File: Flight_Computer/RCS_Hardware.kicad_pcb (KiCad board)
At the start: 2 copper layers, 60 x 53.1 mm, 55 parts, among them J1 SWD, J2 TYPE-C-31-M-12, J4 5V, J5 GND, J8 Conn_01x05_Male, U1 STM32F401CCU6, U2 AMS1117-3.3, U4 BNO055, U5 W25Q32JVSS, U6 MPU-6050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

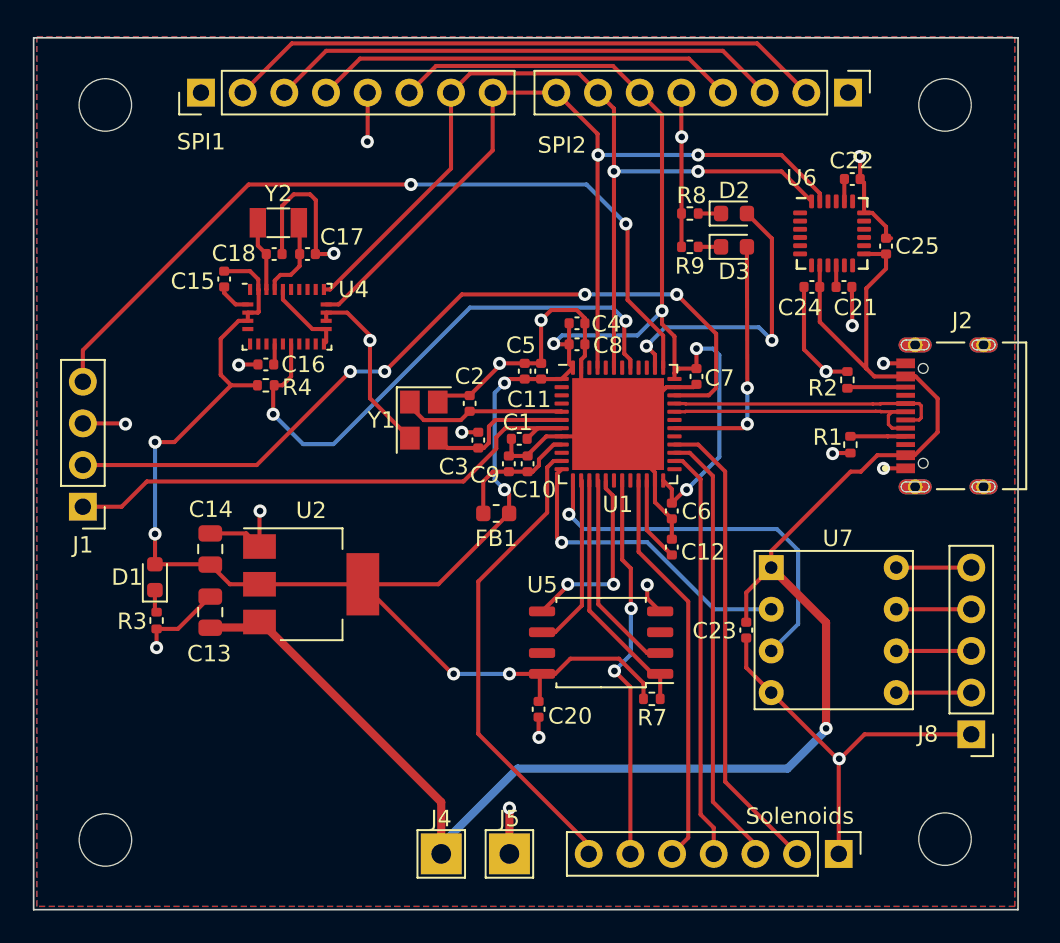
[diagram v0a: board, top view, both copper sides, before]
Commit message: moved some stuff around to aesthetics
moved linear reg down, bottom edge cut & holes up.
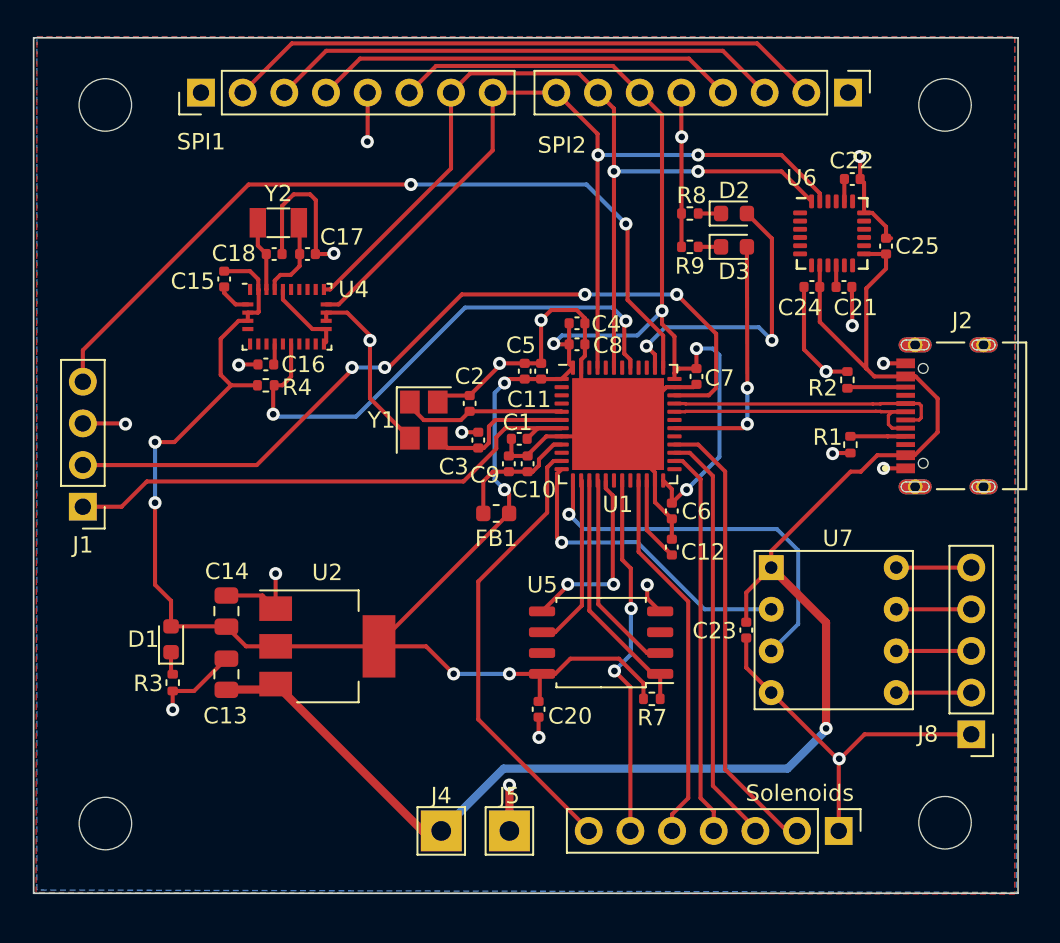
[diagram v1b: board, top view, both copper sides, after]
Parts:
- moved C13 3.91 mm to (113.3, 114.5)
- moved D1 3.91 mm to (110.0, 112.3)
- moved R3 3.91 mm to (110.1, 115.0)
- moved U2 3.91 mm to (119.5, 112.8)
- moved C14 3.91 mm to (113.3, 110.6)
- moved J4 1.40 mm to (126.4, 124.0)
- moved J5 1.40 mm to (130.6, 124.0)
- moved Solenoids 1.40 mm to (150.7, 124.0)
- moved H3 1.00 mm to (106.0, 123.5)
- moved H4 1.00 mm to (157.2, 123.5)
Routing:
- net VBUS: track 102.9 -> 96.4 mm
- net +3.3V: track 146.8 -> 149.2 mm
- net /S6: track 29.4 -> 27.9 mm
- net GND: track 145.5 -> 144.1 mm
- net /S5: track 27.0 -> 25.6 mm
- net /S4: track 25.2 -> 23.8 mm
- net /S3: track 24.4 -> 23.0 mm
- net /BNO_NRST: track 34.1 -> 32.7 mm
- net /S1: track 28.5 -> 27.7 mm
- net /S2: track 23.2 -> 22.4 mm
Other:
- board size 60 x 53.1 mm -> 60 x 52.1 mm

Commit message: uploaded 3d model for components
UCB-C, LTC and Flash Storage
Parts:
- renumbered U7 to LTC
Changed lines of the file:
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@@
     (property "Sheetname" "")
     (attr through_hole)
-    (fp_text reference "U7" (at 4.064 -1.778 unlocked) (layer "F.SilkS")
+    (fp_text reference "LTC" (at 4.064 -1.778 unlocked) (layer "F.SilkS")
         (effects (font (size 1 1) (thickness 0.15)))
     )
@@
     (pad "8" thru_hole circle (at 7.62 0) (size 1.524 1.524) (drill 0.762) (layers "*.Cu" "*.Mask")
       (net 48 "Net-(J8-Pin_5)") (pinfunction "A") (pintype "input"))
+    (model "${KIPRJMOD}/Components/LT1690/LTC1690IN8#PBF.STEP"
+      (offset (xyz 7.6 -7.6 0))
+      (scale (xyz 1 1 1))
+      (rotate (xyz -90 0 0))
+    )
   )
   (footprint "TestPoint:TestPoint_THTPad_2.5x2.5mm_Drill1.2mm" (layer "F.Cu")
@@
     )
     (fp_text user "PCB EDGE" (at 5.2 1.9 90) (layer "F.Fab")
-        (effects (font (size 0.48 0.48) (thickness 0.15)))
+        (effects (font (size 0.48 0.48) (thickness 0.12)))
     )
     (fp_poly
@@
     (pad "S4" thru_hole circle (at 4.325 0 90) (size 0.9 0.9) (drill 0.6) (layers "*.Cu")
       (net 2 "GND") (pinfunction "SHIELD") (pintype "passive"))
+    (model "${KIPRJMOD}/Components/USBC/TYPE-C-31-M-12.step"
+      (offset (xyz 0 0 0))
+      (scale (xyz 1 1 1))
+      (rotate (xyz -90 0 0))
+    )
   )
   (footprint "Crystal:Crystal_SMD_3225-4Pin_3.2x2.5mm" (layer "F.Cu")
@@
     (pad "8" smd roundrect (at 3.6 -1.905 180) (size 1.6 0.6) (layers "F.Cu" "F.Paste" "F.Mask") (roundrect_rratio 0.25)
       (net 5 "+3.3V") (pinfunction "VCC") (pintype "power_in"))
-    (model "${KICAD6_3DMODEL_DIR}/Package_SO.3dshapes/SOIC-8_5.23x5.23mm_P1.27mm.wrl"
+    (model "${KIPRJMOD}/Components/W25Q32/W25Q32JVSSIQ--3DModel-STEP-269445.STEP"
       (offset (xyz 0 0 0))
       (scale (xyz 1 1 1))
-      (rotate (xyz 0 0 0))
+      (rotate (xyz -90 0 0))
     )
   )

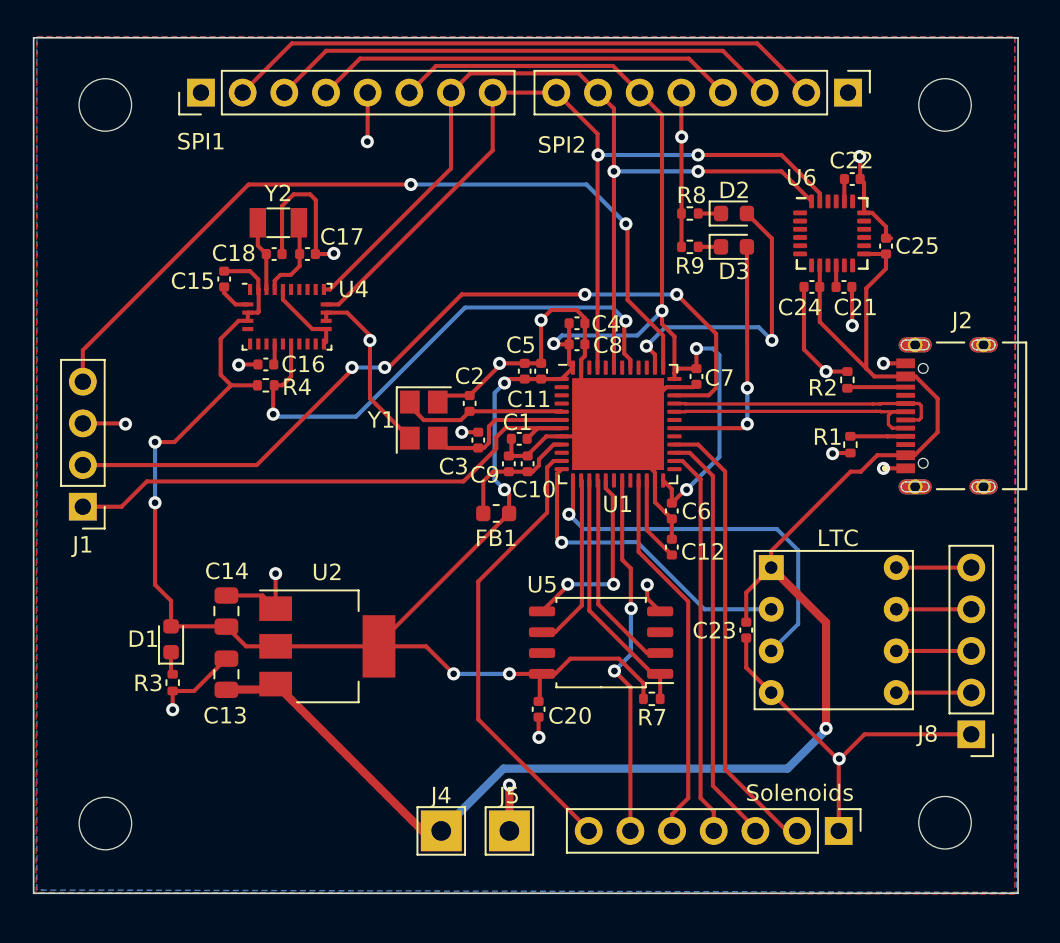
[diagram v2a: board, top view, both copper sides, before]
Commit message: moved SPI connectors down & labeled all pins
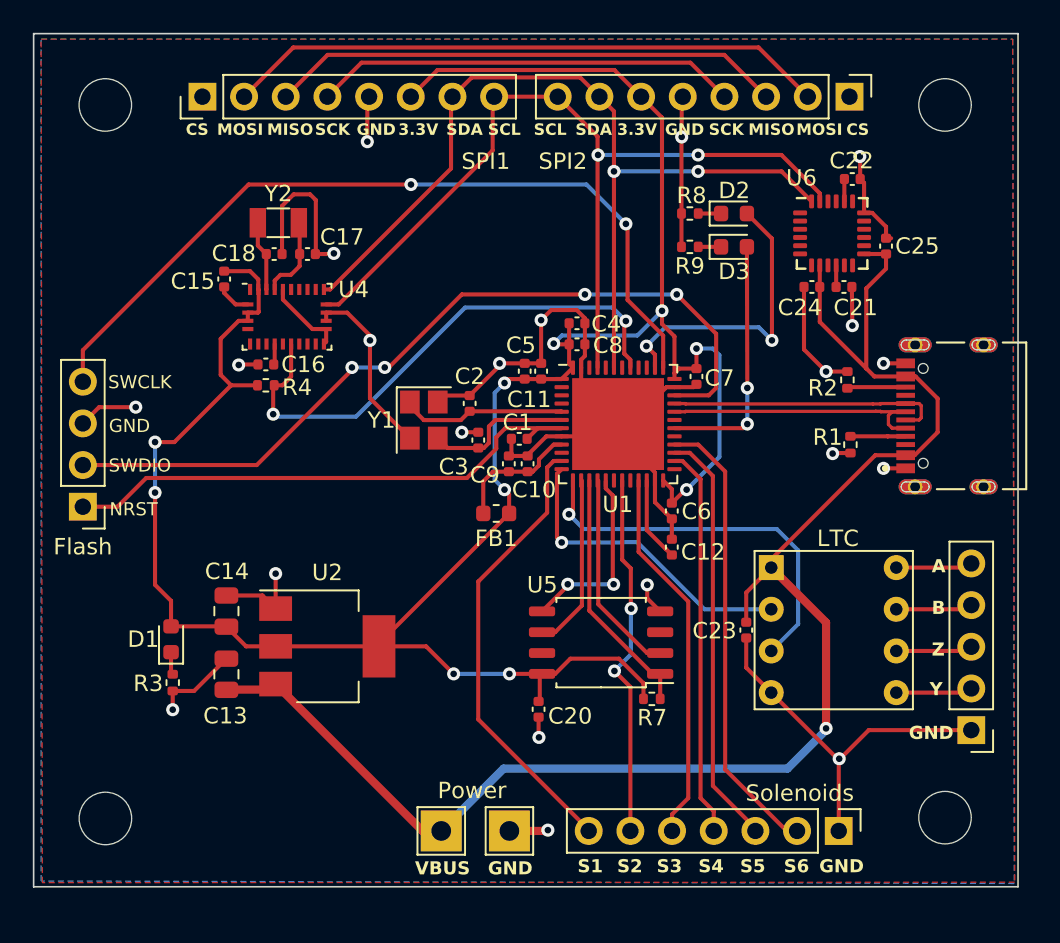
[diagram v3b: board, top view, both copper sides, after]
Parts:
- moved H3 0.31 mm to (106.0, 123.2)
- moved H4 0.31 mm to (157.2, 123.2)
- moved SPI1 0.26 mm to (111.9, 79.2)
- moved SPI2 0.26 mm to (151.3, 79.2)
- moved J8 0.25 mm to (158.8, 117.9)
- renumbered J1 to Flash, J5 to Power
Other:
- board size 60 x 52.1 mm -> 60 x 52 mm
- board text added: "3.3V"
- board text added: "A"
- board text added: "B"
- board text added: "CS"
- board text added: "GND"
- board text added: "MISO"
- board text added: "MOSI"
- board text added: "NRST"
- board text added: "S1"
- board text added: "S2"
- board text added: "S3"
- board text added: "S4"
- board text added: "S5"
- board text added: "S6"
- board text added: "SCK"
- board text added: "SCL"
- board text added: "SDA"
- board text added: "SPI1"
- board text added: "SPI2"
- board text added: "SWCLK"
- board text added: "SWDIO"
- board text added: "VBUS"
- board text added: "Y"
- board text added: "Z"

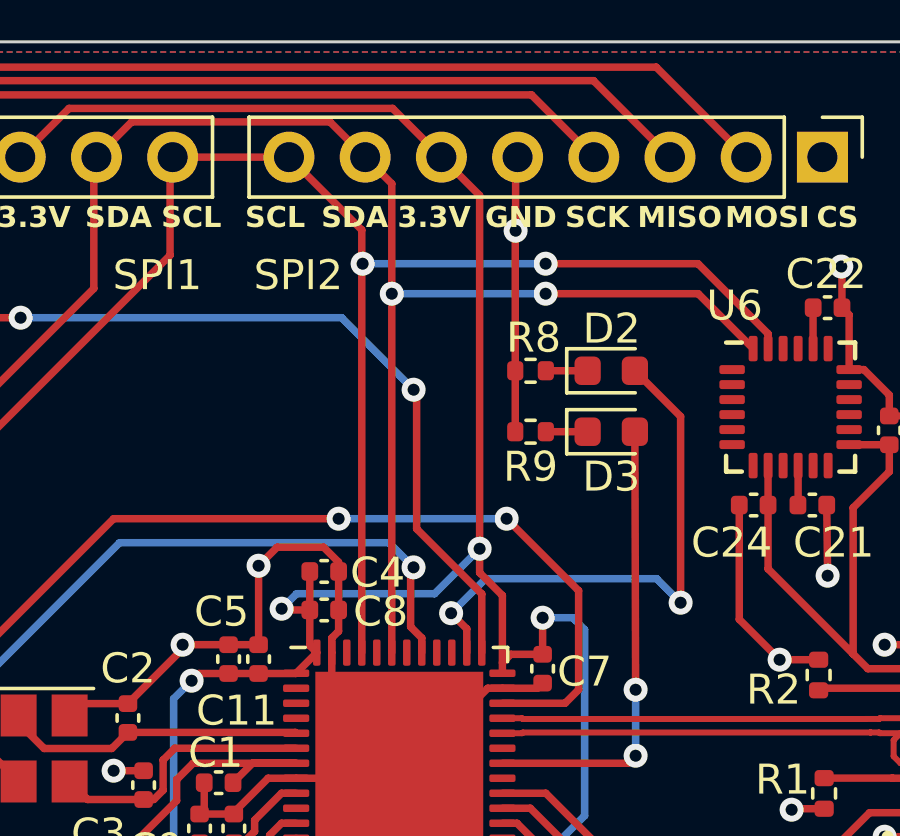
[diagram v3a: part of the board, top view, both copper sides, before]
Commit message: Branding on Back Silckscreen
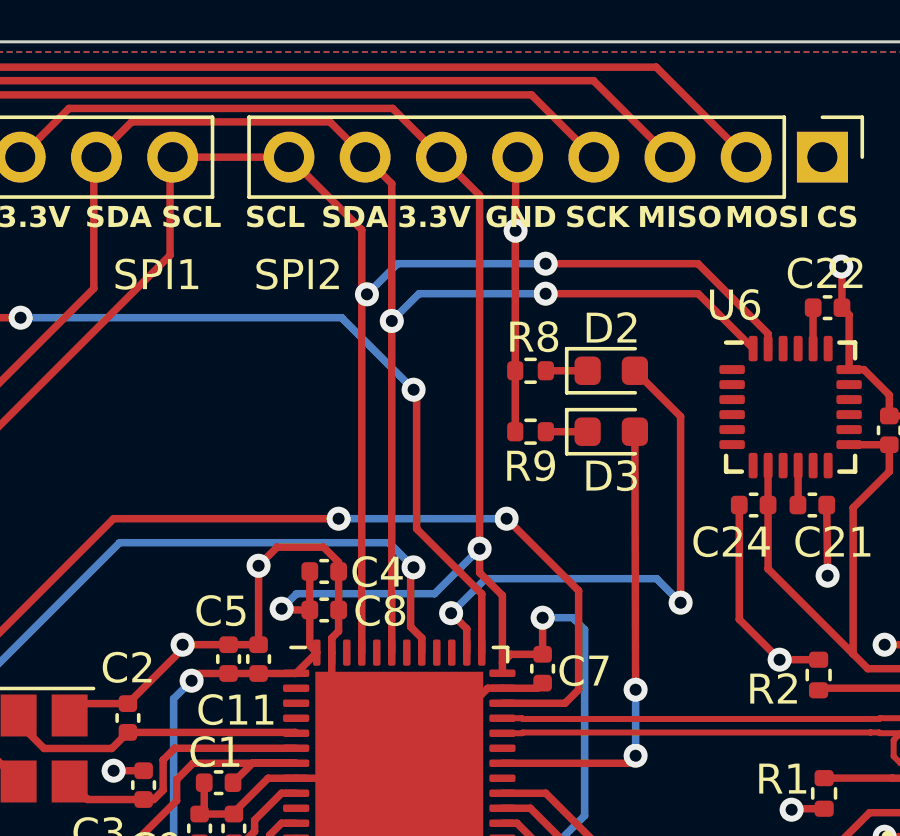
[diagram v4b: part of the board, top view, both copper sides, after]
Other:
- board text added: "Reaction Control System Society For Advanced Rocket Propulsion"
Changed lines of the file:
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@@
   (gr_rect (start 101.6 75.404) (end 161.6 127.404)
     (stroke (width 0.1) (type default)) (fill none) (layer "Edge.Cuts"))
+  (gr_text "Reaction Control System\nSociety For Advanced Rocket Propulsion\n" (at 119.38 120.65) (layer "B.SilkS")
+    (effects (font (size 1 1) (thickness 0.15)) (justify bottom mirror))
+  )
   (gr_text "SPI1" (at 129.159 83.185) (layer "F.SilkS")
     (effects (font (size 1 1) (thickness 0.15)))
@@
   (segment (start 136.875904 92.1) (end 127.9 92.1) (width 0.25) (layer "B.Cu") (net 40))
   (segment (start 127.127 79.248) (end 128.302 78.073) (width 0.25) (layer "F.Cu") (net 41))
-  (segment (start 136.972 83.8) (end 136.972 80.1346) (width 0.25) (layer "F.Cu") (net 41))
+  (segment (start 136.972 84.709) (end 136.972 80.1346) (width 0.25) (layer "F.Cu") (net 41))
   (segment (start 127.04 83.6269) (end 127.04 79.335) (width 0.25) (layer "F.Cu") (net 41))
   (segment (start 128.302 78.073) (end 134.9104 78.073) (width 0.25) (layer "F.Cu") (net 41))
   (segment (start 119.6702 90.9967) (end 127.04 83.6269) (width 0.25) (layer "F.Cu") (net 41))
+  (segment (start 136.972 80.1346) (end 136.0854 79.248) (width 0.25) (layer "F.Cu") (net 41))
   (segment (start 119.2932 90.9967) (end 119.6702 90.9967) (width 0.25) (layer "F.Cu") (net 41))
   (segment (start 127.04 79.335) (end 127.127 79.248) (width 0.25) (layer "F.Cu") (net 41))
   (segment (start 134.9104 78.073) (end 136.0854 79.248) (width 0.25) (layer "F.Cu") (net 41))
   (segment (start 142.1 83.8) (end 147.1872 83.8) (width 0.25) (layer "F.Cu") (net 41))
-  (segment (start 136.972 80.1346) (end 136.0854 79.248) (width 0.25) (layer "F.Cu") (net 41))
-  (segment (start 136.972 95.7637) (end 136.972 83.8) (width 0.25) (layer "F.Cu") (net 41))
+  (segment (start 136.972 95.7637) (end 136.972 84.709) (width 0.25) (layer "F.Cu") (net 41))
   (segment (start 147.1872 83.8) (end 149.0164 85.6292) (width 0.25) (layer "F.Cu") (net 41))
   (segment (start 142.1 83.8) (end 141.9 83.8) (width 0.25) (layer "F.Cu") (net 41))
   (via (at 142.1 83.8) (size 0.8) (drill 0.4) (layers "F.Cu" "B.Cu") (net 41))
-  (via (at 136.972 83.8) (size 0.8) (drill 0.4) (layers "F.Cu" "B.Cu") (net 41))
-  (segment (start 136.972 83.8) (end 142.1 83.8) (width 0.25) (layer "B.Cu") (net 41))
+  (via (at 136.972 84.709) (size 0.8) (drill 0.4) (layers "F.Cu" "B.Cu") (net 41))
+  (segment (start 137.881 83.8) (end 142.1 83.8) (width 0.25) (layer "B.Cu") (net 41))
+  (segment (start 136.972 84.709) (end 137.881 83.8) (width 0.25) (layer "B.Cu") (net 41))
   (segment (start 149.5164 85.136436) (end 147.179964 82.8) (width 0.25) (layer "F.Cu") (net 42))
   (segment (start 149.5164 85.6292) (end 149.5164 85.136436) (width 0.25) (layer "F.Cu") (net 42))
@@
   (segment (start 129.58 79.335) (end 129.667 79.248) (width 0.25) (layer "F.Cu") (net 42))
   (segment (start 120.1908 91.9092) (end 129.58 82.52) (width 0.25) (layer "F.Cu") (net 42))
-  (via (at 136 82.8) (size 0.8) (drill 0.4) (layers "F.Cu" "B.Cu") (net 42))
+  (via (at 136.144 83.82) (size 0.8) (drill 0.4) (layers "F.Cu" "B.Cu") (net 42))
   (via (at 142.1 82.8) (size 0.8) (drill 0.4) (layers "F.Cu" "B.Cu") (net 42))
-  (segment (start 142.1 82.8) (end 136 82.8) (width 0.25) (layer "B.Cu") (net 42))
+  (segment (start 137.164 82.8) (end 136.144 83.82) (width 0.25) (layer "B.Cu") (net 42))
+  (segment (start 142.1 82.8) (end 137.164 82.8) (width 0.25) (layer "B.Cu") (net 42))
   (segment (start 119.507 79.248) (end 121.582 77.173) (width 0.25) (layer "F.Cu") (net 43))
   (segment (start 141.6304 77.173) (end 143.7054 79.248) (width 0.25) (layer "F.Cu") (net 43))
